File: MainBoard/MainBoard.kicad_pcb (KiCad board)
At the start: 2 copper layers, 33.8 x 131 mm, 86 parts, among them J1 Conn_02x04_Odd_Even, SW1 DSHP02TSGET, U1 W25Q16JVUXIQ, U10 VDMR10A1, U11 VDMR10A1, U12 VDMR10A1, U13 74LVC1G34GW,125, U14 SIP32431DR3-T1GE3, U2 RP2040, U3 IS31FL3729-QFLS4-TR, U4 VDMR10A1, U5 VDMR10A1, U6 VDMR10A1, U7 VDMR10A1, U8 VDMR10A1, U9 VDMR10A1, Y1 12.000MHz

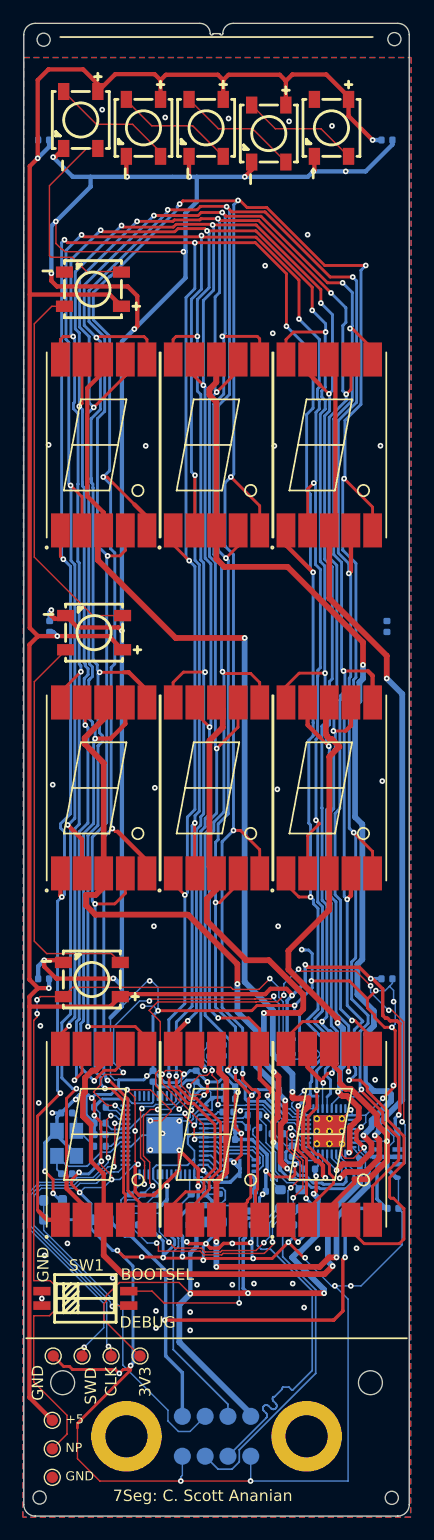
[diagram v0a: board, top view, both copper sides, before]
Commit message: Use 'dumb' 3.1V white LEDs instead of neopixels for legend backlighting
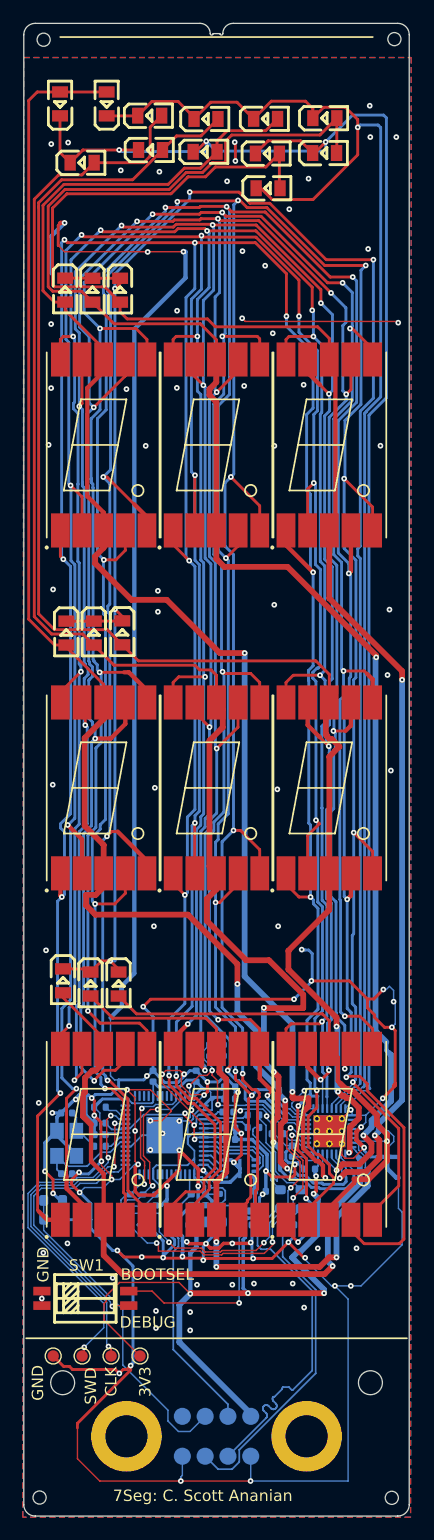
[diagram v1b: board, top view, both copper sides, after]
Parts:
- removed C15: 10uF, Capacitor_SMD:C_0603_1608Metric
- removed C20, C21, C22, C24, C25, C26, C27: 100nF, Capacitor_SMD:C_0402_1005Metric
- removed C23: 1uF, Capacitor_SMD:C_0402_1005Metric
- removed D2: D_TVS, Diode_SMD:D_0402_1005Metric
- removed TP5, TP6, TP7: TestPoint, TestPoint:TestPoint_Pad_D1.0mm
- removed U13: 74LVC1G34GW,125, LCSC:SOT-353_L2.1-W1.3-P0.65-LS2.3-BR
- removed U14: SIP32431DR3-T1GE3, LCSC:SOT-363_L2.0-W1.3-P0.65-LS2.1-BR
- added LED10: KT-0805W, LCSC:LED0805-R-RD, F.Cu at (71.2, 58.4)
- added LED11: KT-0805W, LCSC:LED0805-R-RD, F.Cu at (76.4, 58.3)
- added LED12: KT-0805W, LCSC:LED0805-R-RD, F.Cu at (71.4, 64.5)
- added LED13: KT-0805W, LCSC:LED0805-R-RD, F.Cu at (57.3, 57.1)
- added LED14: KT-0805W, LCSC:LED0805-R-RD, F.Cu at (61.0, 58.1)
- added LED15: KT-0805W, LCSC:LED0805-R-RD, F.Cu at (66.0, 58.4)
- added LED16: KT-0805W, LCSC:LED0805-R-RD, F.Cu at (65.9, 61.3)
- added LED17: KT-0805W, LCSC:LED0805-R-RD, F.Cu at (76.4, 61.4)
- added LED18: KT-0805W, LCSC:LED0805-R-RD, F.Cu at (71.4, 61.4)
- added LED19: KT-0805W, LCSC:LED0805-R-RD, F.Cu at (53.2, 57.1)
- added LED20: KT-0805W, LCSC:LED0805-R-RD, F.Cu at (55.1, 62.2)
- added LED21: KT-0805W, LCSC:LED0805-R-RD, F.Cu at (61.1, 61.1)
- added LED9: KT-0805W, LCSC:LED0805-R-RD, F.Cu at (58.3, 134.3)
- LED1, LED2, LED3, LED4, LED5, LED6, LED7, LED8: value SKC6812RGBW-BW-B -> KT-0805W; footprint LCSC:LED-SMD_4P-L5.0-W5.0-BL_XL-5050RGBC -> LCSC:LED0805-R-RD
- U1: value W25Q16JVUXIQ -> W25Q16JVUXIQ
- moved LED8 78.1 mm to (55.9, 134.3), turned to -90 degrees
- moved LED7 76.5 mm to (53.4, 134.0), turned to -90 degrees
- moved LED1 60.5 mm to (53.6, 73.4), turned to -90 degrees
- moved LED4 45.0 mm to (53.7, 103.5), turned to -90 degrees
- moved LED6 44.9 mm to (58.6, 103.5), turned to -90 degrees
- moved LED5 44.6 mm to (56.1, 103.5), turned to -90 degrees
- moved LED2 30.1 mm to (56.0, 73.4), turned to -90 degrees
- moved LED3 2.38 mm to (58.5, 73.4), turned to -90 degrees
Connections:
- J1 pad 2: +5V -> unconnected-(J1-Pin_2-Pad2)
- LED1 pad 1: +5VP -> /Driver/LED_SW0
- LED1 pad 2: Net-(LED1-DOU) -> /Driver/CS8
- LED2 pad 1: +5VP -> /Driver/LED_SW1
- LED2 pad 2: Net-(LED2-DOU) -> /Driver/CS8
- LED3 pad 1: +5VP -> /Driver/LED_SW2
- LED3 pad 2: Net-(LED3-DOU) -> /Driver/CS8
- LED4 pad 1: +5VP -> /Driver/LED_SW3
- LED4 pad 2: Net-(LED4-DOU) -> /Driver/CS8
- LED5 pad 1: +5VP -> /Driver/LED_SW4
- LED5 pad 2: Net-(LED5-DOU) -> /Driver/CS8
- LED6 pad 1: +5VP -> /Driver/LED_SW5
- LED6 pad 2: Net-(LED6-DOU) -> /Driver/CS8
- LED7 pad 1: +5VP -> /Driver/LED_SW6
- LED7 pad 2: Net-(LED7-DOU) -> /Driver/CS8
- LED8 pad 1: +5VP -> /Driver/LED_SW7
- LED8 pad 2: unconnected-(LED8-DOU-Pad2) -> /Driver/CS8
- U2 pad 27: /NEOPIXEL_3V3 -> unconnected-(U2-GPIO16-Pad27)
- U2 pad 40: /NEOPIXEL_PWR -> unconnected-(U2-GPIO28_ADC2-Pad40)
- U3 pad 6: unconnected-(U3-CS9-Pad6) -> /Driver/CS8
- U3 pad 7: unconnected-(U3-CS10-Pad7) -> /Driver/CS9
- U3 pad 8: unconnected-(U3-CS11-Pad8) -> /Driver/CS10
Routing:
- net +5VP: track 239.2 -> 0.00 mm, vias 8 -> 0
- net /Driver/CS8: track 0.00 -> 183.5 mm, vias 0 -> 5
- net /Driver/CS10: track 0.00 -> 135.2 mm, vias 0 -> 3
- net /Driver/CS9: track 0.00 -> 131.1 mm, vias 0 -> 1
- net /Driver/LED_SW5: track 46.0 -> 130.7 mm
- net GND: track 582.5 -> 500.5 mm, vias 117 -> 125
- net /NEOPIXEL: track 73.2 -> 0.00 mm, vias 3 -> 0
- net /Driver/LED_SW4: track 61.5 -> 134.6 mm
- net /Driver/LED_SW3: track 64.5 -> 127.8 mm
- net /Driver/LED_SW2: track 81.1 -> 141.4 mm
- net /Driver/LED_SW1: track 88.7 -> 144.7 mm
- net +5V: track 53.9 -> 0.00 mm, vias 2 -> 0
- net /NEOPIXEL_PWR: track 51.4 -> 0.00 mm, vias 6 -> 0
- net /Driver/LED_SW0: track 88.5 -> 128.8 mm
- net /NEOPIXEL_3V3: track 37.0 -> 0.00 mm, vias 4 -> 0
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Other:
- board text added: "7-Segment Input Module 2023 Framework CC BY 4.0 2024 C. Scott Ananian 2024-07-25"
- board text removed: "+5"
- board text removed: "7-Segment Input Module 2023 Framework CC BY 4.0 2024 C. Scott Ananian 2024-07-13"
- board text removed: "NP"
